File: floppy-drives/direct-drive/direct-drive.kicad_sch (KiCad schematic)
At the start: 18 parts, among them J1 Floppy Drive, J2 Control, SW1 Reset, SW2 User, U1 ATtiny24A-P, U2 TXU0304PWR, Y1 DSC1001A

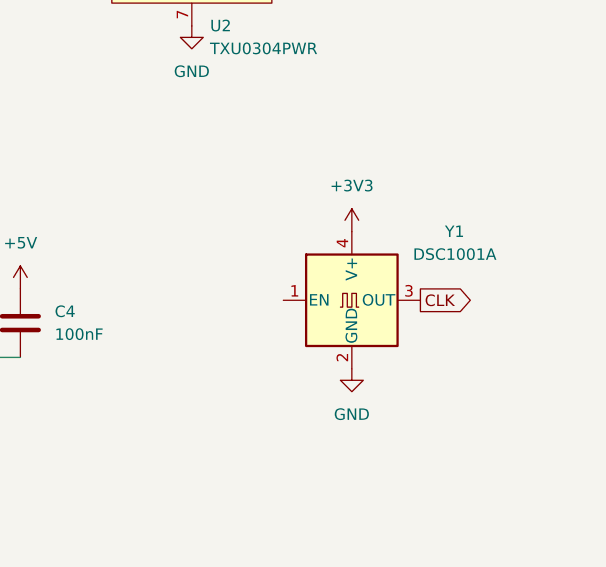
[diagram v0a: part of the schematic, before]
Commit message: Replace 7050 oscillator with 3225 and draft a PCB
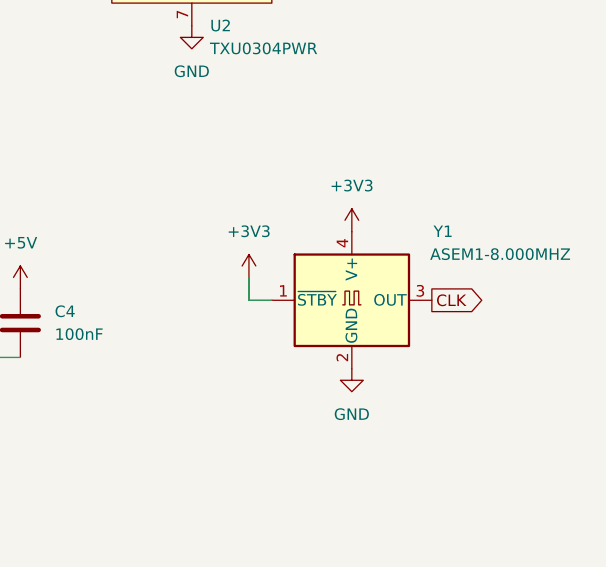
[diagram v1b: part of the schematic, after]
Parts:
- Y1: value DSC1001A -> ASEM1-8.000MHZ; footprint agausmann:DSC1001A-4Pin-7.0x5.0mm -> agausmann:ASEM-4Pin-3.2x2.5mm; symbol agausmann:DSC1001A -> agausmann:ASEM
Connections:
- net +3V3: now also Y1.1 (~{STBY})
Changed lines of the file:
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@@
+    (stroke (width 0) (type default) (color 0 0 0 0))
+  )
+  (wire (pts (xy 204.47 105.41) (xy 207.01 105.41))
     (stroke (width 0) (type default) (color 0 0 0 0))
   )
@@
   )
   (wire (pts (xy 30.48 64.77) (xy 30.48 67.31))
+    (stroke (width 0) (type default) (color 0 0 0 0))
+  )
+  (wire (pts (xy 204.47 102.87) (xy 204.47 105.41))
     (stroke (width 0) (type default) (color 0 0 0 0))
   )
@@
     )
   )
-  (global_label "CLK" (shape output) (at 223.52 105.41 0) (fields_autoplaced)
-    (effects (font (size 1.27 1.27)) (justify left))
-    (property "Intersheet References" "${INTERSHEET_REFS}" (id 0) (at 229.5012 105.3306 0)
+  (global_label "CLK" (shape output) (at 224.79 105.41 0) (fields_autoplaced)
+    (effects (font (size 1.27 1.27)) (justify left))
+    (property "Intersheet References" "${INTERSHEET_REFS}" (id 0) (at 230.7712 105.3306 0)
       (effects (font (size 1.27 1.27)) (justify left) hide)
     )
@@
     (pin "1")
     (pin "2")
+  )
+  (symbol (lib_id "power:+3V3") (at 204.47 102.87 0) (unit 1)
+    (in_bom yes) (on_board yes)
+    (property "Reference" "#PWR?" (id 0) (at 204.47 106.68 0)
+      (effects (font (size 1.27 1.27)) hide)
+    )
+    (property "Value" "+3V3" (id 1) (at 204.47 97.79 0))
+    (property "Footprint" "" (id 2) (at 204.47 102.87 0)
+      (effects (font (size 1.27 1.27)) hide)
+    )
+    (property "Datasheet" "" (id 3) (at 204.47 102.87 0)
+      (effects (font (size 1.27 1.27)) hide)
+    )
+    (pin "1")
   )
   (symbol (lib_id "Connector_Generic:Conn_02x05_Odd_Even") (at 66.04 34.29 0) (unit 1)
@@
     (pin "1")
   )
-  (symbol (lib_id "agausmann:DSC1001A") (at 215.9 105.41 0) (unit 1)
+  (symbol (lib_id "agausmann:ASEM") (at 215.9 105.41 0) (unit 1)
     (in_bom yes) (on_board yes)
-    (property "Reference" "Y1" (id 0) (at 227.33 97.79 0))
-    (property "Value" "DSC1001A" (id 1) (at 227.33 100.33 0))
-    (property "Footprint" "agausmann:DSC1001A-4Pin-7.0x5.0mm" (id 2) (at 245.11 115.57 0)
-      (effects (font (size 1.27 1.27)) hide)
-    )
-    (property "Datasheet" "https://rocelec.widen.net/view/pdf/4jp9qpy8qv/MCHP-S-A0003587227-1.pdf" (id 3) (at 245.11 118.11 0)
+    (property "Reference" "Y1" (id 0) (at 226.06 97.79 0))
+    (property "Value" "ASEM1-8.000MHZ" (id 1) (at 232.41 100.33 0))
+    (property "Footprint" "agausmann:ASEM-4Pin-3.2x2.5mm" (id 2) (at 245.11 115.57 0)
+      (effects (font (size 1.27 1.27)) hide)
+    )
+    (property "Datasheet" "https://abracon.com/Oscillators/ASEM.pdf" (id 3) (at 245.11 118.11 0)
       (effects (font (size 1.27 1.27)) hide)
     )
@@
       (reference "#PWR022") (unit 1) (value "GND") (footprint "")
     )
+    (path "/06ad25d7-870f-4ddb-a7c8-8a6709df2212"
+      (reference "#PWR?") (unit 1) (value "+3V3") (footprint "")
+    )
     (path "/e4628a3c-66b2-47fc-abc7-0e1662732465"
       (reference "C1") (unit 1) (value "100nF") (footprint "Capacitor_SMD:C_0603_1608Metric")
@@
     )
     (path "/58c98dc4-3aab-448f-a38f-0f6c53ff8473"
-      (reference "Y1") (unit 1) (value "DSC1001A") (footprint "agausmann:DSC1001A-4Pin-7.0x5.0mm")
-    )
-  )
+      (reference "Y1") (unit 1) (value "ASEM1-8.000MHZ") (footprint "agausmann:ASEM-4Pin-3.2x2.5mm")
+    )
+  )

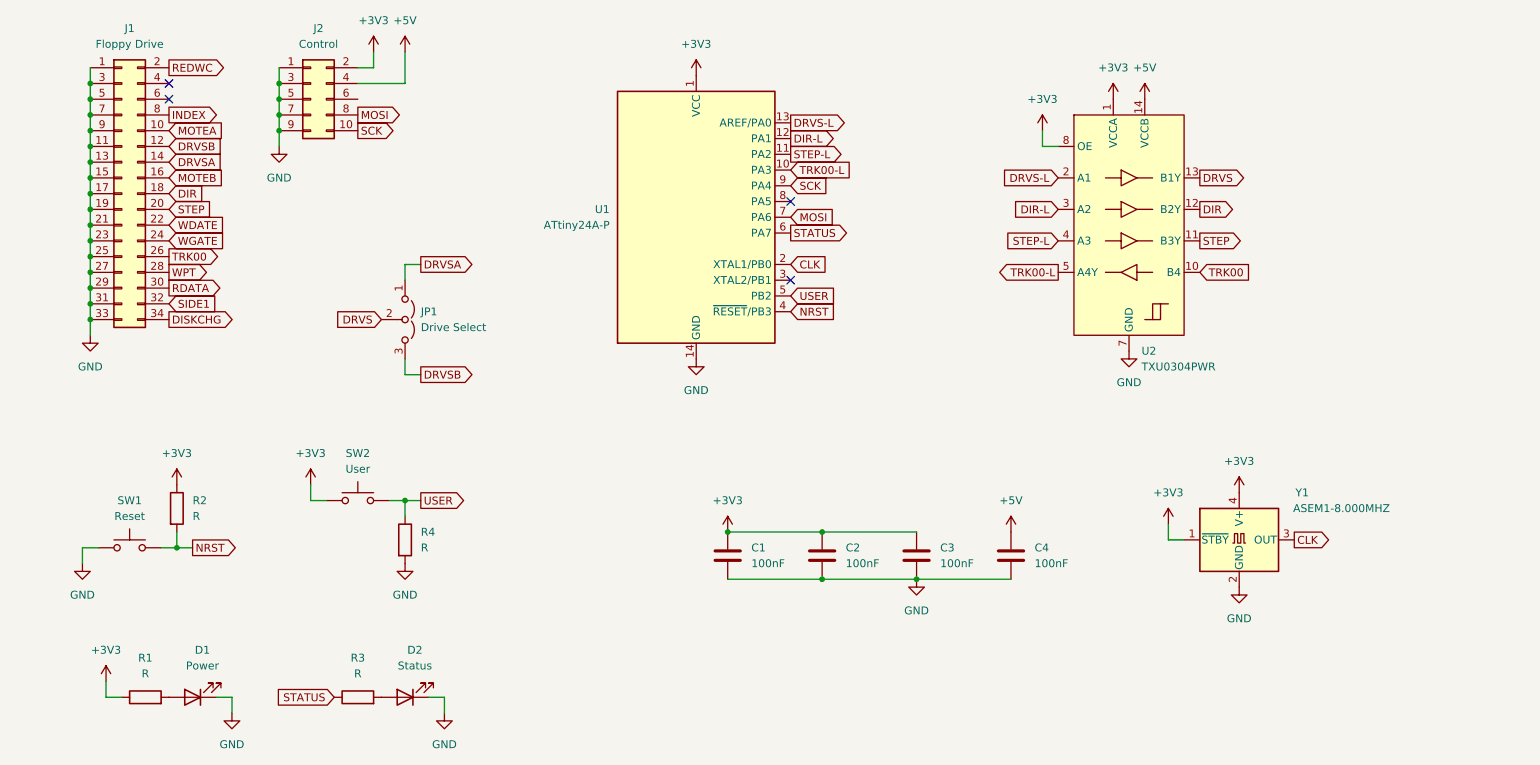
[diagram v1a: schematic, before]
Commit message: direct-drive schematic: Fix XO cap value and place caps near their corresponding chips.
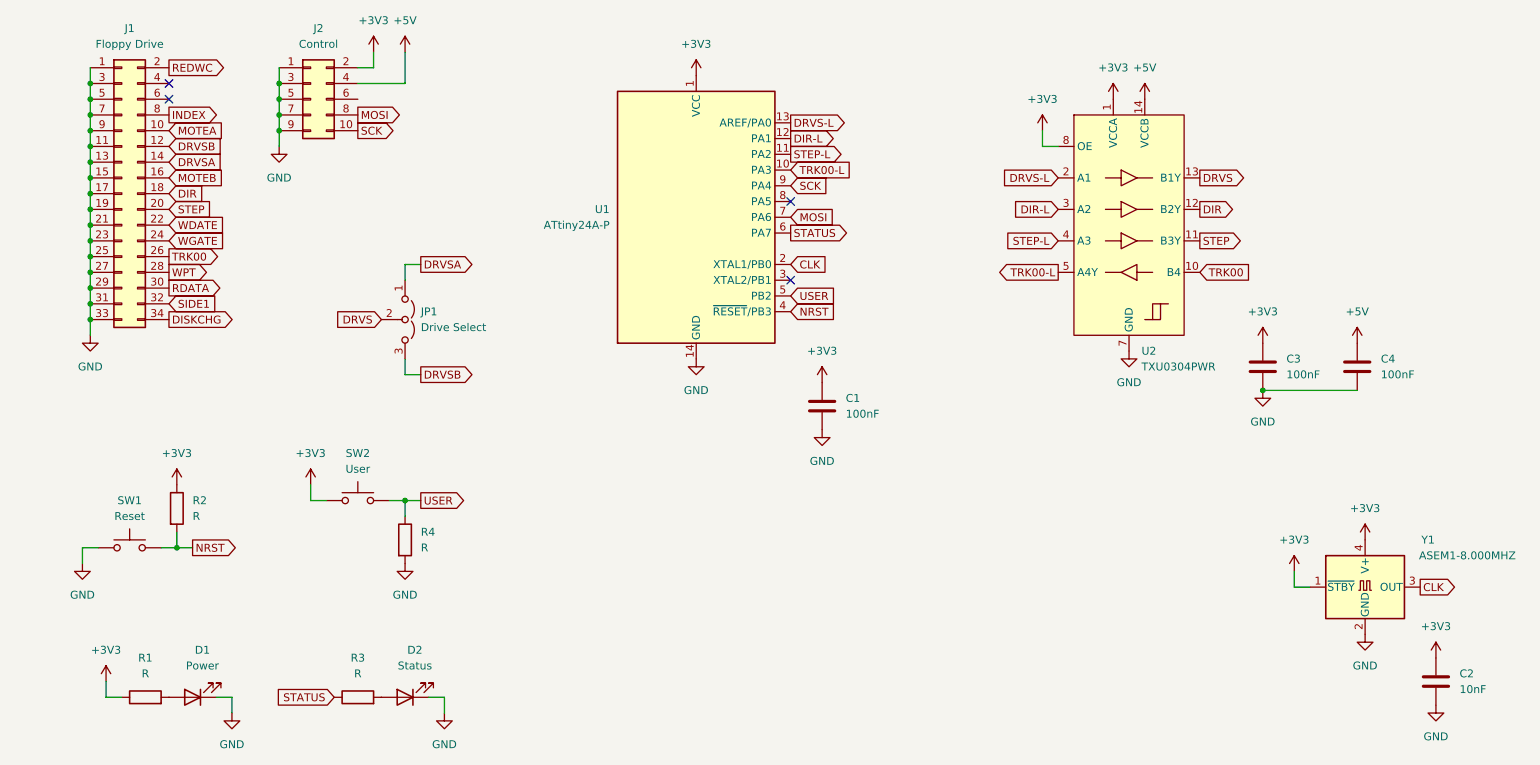
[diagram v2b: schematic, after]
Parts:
- C2: value 100nF -> 10nF
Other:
- moved on the sheet: C1, C2, C3, C4, Y1

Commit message: Add Digikey part numbers and missing 3D models
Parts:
- C1, C3, C4: Digikey (none) -> 1276-1005-1-ND
- C2: Digikey (none) -> 1276-1926-1-ND
- D1: Digikey (none) -> 732-4978-1-ND
- D2: Digikey (none) -> 732-4971-1-ND
- J1: Digikey (none) -> S9207-ND
- J2: Digikey (none) -> ED10533-ND
- R2, R4: value R -> 10k
- SW1, SW2: Digikey (none) -> CKN10880CT-ND
- U1: Comment (none) -> Socketed; Digikey (none) -> ED3045-5-ND
- U2: Digikey (none) -> 296-TXU0304PWRCT-ND
- Y1: Digikey (none) -> 535-9754-1-ND
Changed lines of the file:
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@@
+      (effects (font (size 1.27 1.27)) hide)
+    )
+    (property "Digikey" "CKN10880CT-ND" (id 4) (at 73.66 99.06 0)
       (effects (font (size 1.27 1.27)) hide)
     )
@@
     )
     (property "Datasheet" "~" (id 3) (at 66.04 34.29 0)
+      (effects (font (size 1.27 1.27)) hide)
+    )
+    (property "Digikey" "ED10533-ND" (id 4) (at 66.04 34.29 0)
       (effects (font (size 1.27 1.27)) hide)
     )
@@
       (effects (font (size 1.27 1.27)) hide)
     )
+    (property "Digikey" "732-4978-1-ND" (id 4) (at 46.99 130.81 0)
+      (effects (font (size 1.27 1.27)) hide)
+    )
     (pin "1")
     (pin "2")
@@
     )
     (property "Datasheet" "~" (id 3) (at 35.56 49.53 0)
+      (effects (font (size 1.27 1.27)) hide)
+    )
+    (property "Digikey" "S9207-ND" (id 4) (at 35.56 49.53 0)
       (effects (font (size 1.27 1.27)) hide)
     )
@@
   (symbol (lib_id "power:GND") (at 247.65 132.08 0) (unit 1)
     (in_bom yes) (on_board yes) (fields_autoplaced)
-    (property "Reference" "#PWR?" (id 0) (at 247.65 138.43 0)
+    (property "Reference" "#PWR0102" (id 0) (at 247.65 138.43 0)
       (effects (font (size 1.27 1.27)) hide)
     )
@@
     )
     (property "Datasheet" "http://ww1.microchip.com/downloads/en/DeviceDoc/doc8183.pdf" (id 3) (at 128.27 53.34 0)
+      (effects (font (size 1.27 1.27)) hide)
+    )
+    (property "Comment" "Socketed" (id 4) (at 128.27 53.34 0)
+      (effects (font (size 1.27 1.27)) hide)
+    )
+    (property "Digikey" "ED3045-5-ND" (id 5) (at 128.27 53.34 0)
       (effects (font (size 1.27 1.27)) hide)
     )
@@
   (symbol (lib_id "power:+3V3") (at 247.65 124.46 0) (unit 1)
     (in_bom yes) (on_board yes) (fields_autoplaced)
-    (property "Reference" "#PWR?" (id 0) (at 247.65 128.27 0)
+    (property "Reference" "#PWR0103" (id 0) (at 247.65 128.27 0)
       (effects (font (size 1.27 1.27)) hide)
     )
@@
       (effects (font (size 1.27 1.27)) hide)
     )
+    (property "Digikey" "535-9754-1-ND" (id 4) (at 236.22 113.03 0)
+      (effects (font (size 1.27 1.27)) hide)
+    )
     (pin "1")
     (pin "2")
@@
   (symbol (lib_id "power:+3V3") (at 219.71 73.66 0) (unit 1)
     (in_bom yes) (on_board yes) (fields_autoplaced)
-    (property "Reference" "#PWR?" (id 0) (at 219.71 77.47 0)
+    (property "Reference" "#PWR0104" (id 0) (at 219.71 77.47 0)
       (effects (font (size 1.27 1.27)) hide)
     )
@@
   (symbol (lib_id "power:GND") (at 219.71 81.28 0) (unit 1)
     (in_bom yes) (on_board yes) (fields_autoplaced)
-    (property "Reference" "#PWR?" (id 0) (at 219.71 87.63 0)
+    (property "Reference" "#PWR0105" (id 0) (at 219.71 87.63 0)
       (effects (font (size 1.27 1.27)) hide)
     )
@@
       (effects (font (size 1.27 1.27)) hide)
     )
+    (property "Digikey" "1276-1005-1-ND" (id 4) (at 219.71 77.47 0)
+      (effects (font (size 1.27 1.27)) hide)
+    )
     (pin "1")
     (pin "2")
@@
       (effects (font (size 1.27 1.27)) hide)
     )
+    (property "Digikey" "1276-1926-1-ND" (id 4) (at 247.65 128.27 0)
+      (effects (font (size 1.27 1.27)) hide)
+    )
     (pin "1")
     (pin "2")
@@
       (effects (font (size 1.27 1.27)) (justify left))
     )
-    (property "Value" "R" (id 1) (at 46.99 101.5999 0)
+    (property "Value" "10k" (id 1) (at 46.99 101.5999 0)
       (effects (font (size 1.27 1.27)) (justify left))
     )
@@
       (effects (font (size 1.27 1.27)) hide)
     )
+    (property "Digikey" "732-4971-1-ND" (id 4) (at 81.28 130.81 0)
+      (effects (font (size 1.27 1.27)) hide)
+    )
     (pin "1")
     (pin "2")
@@
       (effects (font (size 1.27 1.27)) hide)
     )
+    (property "Digikey" "CKN10880CT-ND" (id 4) (at 36.83 106.68 0)
+      (effects (font (size 1.27 1.27)) hide)
+    )
     (pin "1")
     (pin "2")
@@
     )
     (property "Datasheet" "https://www.ti.com/lit/ds/symlink/txu0304.pdf" (id 3) (at 231.14 35.56 0)
+      (effects (font (size 1.27 1.27)) hide)
+    )
+    (property "Digikey" "296-TXU0304PWRCT-ND" (id 4) (at 198.12 44.45 0)
       (effects (font (size 1.27 1.27)) hide)
     )
@@
       (effects (font (size 1.27 1.27)) (justify left))
     )
-    (property "Value" "R" (id 1) (at 83.82 106.6799 0)
+    (property "Value" "10k" (id 1) (at 83.82 106.6799 0)
       (effects (font (size 1.27 1.27)) (justify left))
     )
@@
     )
     (property "Datasheet" "~" (id 3) (at 234.95 77.47 0)
+      (effects (font (size 1.27 1.27)) hide)
+    )
+    (property "Digikey" "1276-1005-1-ND" (id 4) (at 234.95 77.47 0)
       (effects (font (size 1.27 1.27)) hide)
     )
@@
     )
     (property "Datasheet" "~" (id 3) (at 148.59 83.82 0)
+      (effects (font (size 1.27 1.27)) hide)
+    )
+    (property "Digikey" "1276-1005-1-ND" (id 4) (at 148.59 83.82 0)
       (effects (font (size 1.27 1.27)) hide)
     )
@@
     )
     (path "/31092ca9-4169-40f8-aca6-77c10996868f"
-      (reference "#PWR?") (unit 1) (value "GND") (footprint "")
+      (reference "#PWR0102") (unit 1) (value "GND") (footprint "")
     )
     (path "/417539cc-1a8a-4755-9d32-af54f5430be2"
-      (reference "#PWR?") (unit 1) (value "+3V3") (footprint "")
+      (reference "#PWR0103") (unit 1) (value "+3V3") (footprint "")
     )
     (path "/97117e48-6b5f-4f05-9867-3a9354d202c7"
-      (reference "#PWR?") (unit 1) (value "+3V3") (footprint "")
+      (reference "#PWR0104") (unit 1) (value "+3V3") (footprint "")
     )
     (path "/9926784f-8c13-4345-a3e1-8673199f7424"
-      (reference "#PWR?") (unit 1) (value "GND") (footprint "")
+      (reference "#PWR0105") (unit 1) (value "GND") (footprint "")
     )
     (path "/e4628a3c-66b2-47fc-abc7-0e1662732465"
@@
     )
     (path "/c3798c58-fd3e-4711-8d0b-b8b7db367814"
-      (reference "R2") (unit 1) (value "R") (footprint "Resistor_SMD:R_0603_1608Metric")
+      (reference "R2") (unit 1) (value "10k") (footprint "Resistor_SMD:R_0603_1608Metric")
     )
     (path "/32aa7c6b-1026-4563-adee-de5b02e61bef"
@@
     )
     (path "/d815769b-9f39-401b-8248-4972824d46e1"
-      (reference "R4") (unit 1) (value "R") (footprint "Resistor_SMD:R_0603_1608Metric")
+      (reference "R4") (unit 1) (value "10k") (footprint "Resistor_SMD:R_0603_1608Metric")
     )
     (path "/cafcdbe3-93b1-4cd8-9d63-b7a2ffc721bc"

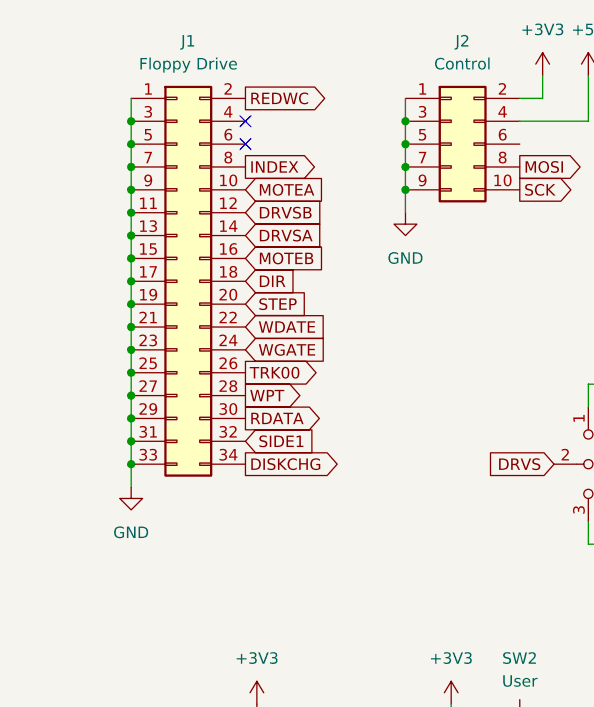
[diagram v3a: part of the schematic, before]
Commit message: direct-drive: Update schematic to use custom Conn_FloppyDrive symbol
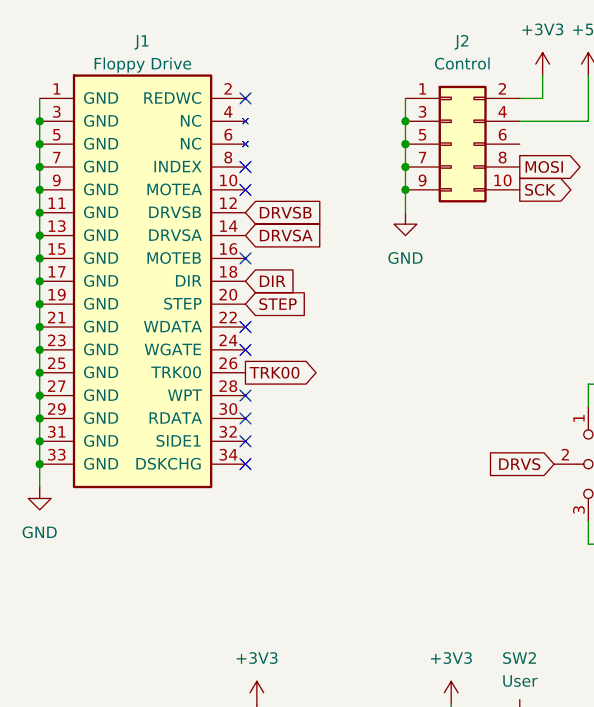
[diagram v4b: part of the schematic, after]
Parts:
- J1: symbol Connector_Generic:Conn_02x17_Odd_Even -> agausmann:Conn_FloppyDrive
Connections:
- net DISKCHG: no longer names the net of J1.34 (DSKCHG)
- net INDEX: no longer names the net of J1.8 (INDEX)
- net MOTEA: no longer names the net of J1.10 (MOTEA)
- net MOTEB: no longer names the net of J1.16 (MOTEB)
- net RDATA: no longer names the net of J1.30 (RDATA)
- net REDWC: no longer names the net of J1.2 (REDWC)
- net SIDE1: no longer names the net of J1.32 (SIDE1)
- net WDATE: no longer names the net of J1.22 (WDATA)
- net WGATE: no longer names the net of J1.24 (WGATE)
- net WPT: no longer names the net of J1.28 (WPT)
- no-connect marks 4 -> 12
